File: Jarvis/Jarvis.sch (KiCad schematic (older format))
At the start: 180 parts, among them IC1 ADP1607, IC2 MAX-8Q, IC3 MPU-9250, IC4 STM32F411CxUx, IC5 Si4460, IC6 MS5611-01BA03, IC7 S25FL127S, J1 PYRO, J2 PWR, J3 ARM, J4 MICROUSB, P1 SMA, P2 SMA, P3 SWD_TC, Q1 PFET, Q2 PFET, Q3 PFET, Q4 NFET, Q5 NFET, Q6 NFET, Q7 NFET, X1 434MHz ANT, X10 Housing x1, X11 Housing x3, X12 M Crimps x6, X13 F Crimps x17, X14 Crimp Tool, X15 RF Frame, X16 RF Cover, X2 Red LED, X3 AA Battery, X4 AA Holder, X5 ARM Switch, X6 Wire, X7 Heat Shrink, X8 Housing x1, X9 Housing x4, Y1 26MHz, Y2 30MHz

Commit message: Checked all Footprints
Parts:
- added X17, X18, X19: Heat Shrink, symbol PART
- C11: Farnell 2524673 -> 1414575
- C27: Farnell 1973025 -> 2496795
- D1, D2, D3: Farnell 1226372 -> 1328306
- D4: Farnell 1226390 -> 1328309
- IC7: footprint agg:WND008 -> agg:S25FL127S
- L1: footprint Inductors_NEOSID:Neosid_Inductor_SM-NE29_SMD1008 -> Library:VLF252012MT
- P2: Farnell 1608592 -> 1019325
- R10, R26, R29, R33, R34, R4, R5, R6, R8, R9: Farnell 1358015 -> 2072515
- X12: Farnell (none) -> 1830754
- X13: RS (none) -> 688-1381
- X6: Farnell (none) -> 2367724
- X7: Farnell (none) -> 1210349
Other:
- note added: "X1 434MHz Stubby Radio Antenna\nX2 Red Indicator LED for Pyro Arming\nX3 Energizer L91 Lithium Ultimate AA\nX4 AA Battery Holder\nX5 Key Switch for Arming Pyrotechnics\nX6 Wire\nX7 Black Heatshrink"
- note added: "X17 Red Heatshrink\nX18 Blue Heatshrink\nX19 Yellow Heatshrink"
- note removed: "TODO:"
- note removed: "TODO: Select Wire, Heatshrink & Crimps"
- note removed: "X1 434MHz Stubby Radio Antenna\nX2 Red Indicator LED for Pyro Arming\nX3 Energizer L91 Lithium Ultimate AA\nX4 AA Battery Holder\nX5 Key Switch for Arming Pyrotechnics\nX6 Wire\nX7 Heatshrink"
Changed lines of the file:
@@
 F 0 "L1" H 1630 990 50  0000 L CNN
 F 1 "2.2uH" H 1650 900 50  0000 L CNN
-F 2 "Inductors_NEOSID:Neosid_Inductor_SM-NE29_SMD1008" H 1600 950 50  0001 C CNN
+F 2 "Library:VLF252012MT" H 1600 950 50  0001 C CNN
 F 3 "http://www.farnell.com/datasheets/1759590.pdf" H 1600 950 50  0001 C CNN
 F 4 "2455292" H 1600 950 60  0001 C CNN "Farnell"
@@
 F 2 "agg:0402-L" H 2000 5800 50  0001 C CNN
 F 3 "http://www.farnell.com/datasheets/1729045.pdf" H 2000 5800 50  0001 C CNN
-F 4 "1358015" H 2000 5800 60  0001 C CNN "Farnell"
+F 4 "2072515" H 2000 5800 60  0001 C CNN "Farnell"
 	1    2000 5800
 	0    -1   1    0
@@
 Text Label 11700 4750 0    60   ~ 0
 PYRO3
-Text Notes 7550 9220 0    47   ~ 0
+Text Notes 8450 9220 0    47   ~ 0
 Camera will have its\nown power supply ect.
 $Comp
@@
 F 2 "agg:0603-LED" H 12650 4800 50  0001 C CNN
 F 3 "http://www.farnell.com/datasheets/1693302.pdf" H 12650 4800 50  0001 C CNN
-F 4 "1226372" H 12650 4800 60  0001 C CNN "Farnell"
+F 4 "1328306" H 12650 4800 60  0001 C CNN "Farnell"
 	1    12650 4800
 	0    -1   -1   0
@@
 F 2 "agg:0603-LED" H 15000 4800 50  0001 C CNN
 F 3 "http://www.farnell.com/datasheets/302470.pdf" H 15000 4800 50  0001 C CNN
-F 4 "1226390" H 15000 4800 60  0001 C CNN "Farnell"
+F 4 "1328309" H 15000 4800 60  0001 C CNN "Farnell"
 	1    15000 4800
 	0    -1   -1   0
@@
 F 2 "agg:0402-L" H 7300 6750 50  0001 C CNN
 F 3 "http://www.farnell.com/datasheets/1446011.pdf" H 7300 6750 50  0001 C CNN
-F 4 "1973025" H 7300 6750 60  0001 C CNN "Farnell"
+F 4 "2496795" H 7300 6750 60  0001 C CNN "Farnell"
 	1    7300 6750
 	1    0    0    -1
@@
 F 2 "Library:SMA-142-0701-801" H 8300 6600 60  0001 C CNN
 F 3 "http://www.farnell.com/datasheets/493539.pdf" H 8300 6600 60  0001 C CNN
-F 4 "1608592" H 8300 6600 60  0001 C CNN "Farnell"
+F 4 "1019325" H 8300 6600 60  0001 C CNN "Farnell"
 	1    8300 6600
 	1    0    0    1
@@
 F 2 "agg:0402-L" H 5200 3900 50  0001 C CNN
 F 3 "http://www.farnell.com/datasheets/2009679.pdf" H 5200 3900 50  0001 C CNN
-F 4 "2524673" H 5200 3900 60  0001 C CNN "Farnell"
+F 4 "1414575" H 5200 3900 60  0001 C CNN "Farnell"
 	1    5200 3900
 	-1   0    0    -1
@@
 F 2 "agg:0402-L" H 10050 7000 50  0001 C CNN
 F 3 "http://www.farnell.com/datasheets/1729045.pdf" H 10050 7000 50  0001 C CNN
-F 4 "1358015" H 10050 7000 60  0001 C CNN "Farnell"
+F 4 "2072515" H 10050 7000 60  0001 C CNN "Farnell"
 	1    10050 7000
 	0    -1   1    0
@@
 F 2 "agg:0402-L" H 10350 6600 50  0001 C CNN
 F 3 "http://www.farnell.com/datasheets/1729045.pdf" H 10350 6600 50  0001 C CNN
-F 4 "1358015" H 10350 6600 60  0001 C CNN "Farnell"
+F 4 "2072515" H 10350 6600 60  0001 C CNN "Farnell"
 	1    10350 6600
 	-1   0    0    -1
@@
 F 2 "agg:0603-LED" H 13450 4800 50  0001 C CNN
 F 3 "http://www.farnell.com/datasheets/1693302.pdf" H 13450 4800 50  0001 C CNN
-F 4 "1226372" H 13450 4800 60  0001 C CNN "Farnell"
+F 4 "1328306" H 13450 4800 60  0001 C CNN "Farnell"
 	1    13450 4800
 	0    -1   -1   0
@@
 F 2 "agg:0603-LED" H 14200 4800 50  0001 C CNN
 F 3 "http://www.farnell.com/datasheets/1693302.pdf" H 14200 4800 50  0001 C CNN
-F 4 "1226372" H 14200 4800 60  0001 C CNN "Farnell"
+F 4 "1328306" H 14200 4800 60  0001 C CNN "Farnell"
 	1    14200 4800
 	0    -1   -1   0
@@
 F 2 "agg:0402-L" H 9400 1600 50  0001 C CNN
 F 3 "http://www.farnell.com/datasheets/1729045.pdf" H 9400 1600 50  0001 C CNN
-F 4 "1358015" H 9400 1600 60  0001 C CNN "Farnell"
+F 4 "2072515" H 9400 1600 60  0001 C CNN "Farnell"
 	1    9400 1600
 	0    -1   -1   0
@@
 F 2 "agg:0402-L" H 11850 1600 50  0001 C CNN
 F 3 "http://www.farnell.com/datasheets/1729045.pdf" H 11850 1600 50  0001 C CNN
-F 4 "1358015" H 11850 1600 60  0001 C CNN "Farnell"
+F 4 "2072515" H 11850 1600 60  0001 C CNN "Farnell"
 	1    11850 1600
 	0    -1   -1   0
@@
 F 2 "agg:0402-L" H 14300 1600 50  0001 C CNN
 F 3 "http://www.farnell.com/datasheets/1729045.pdf" H 14300 1600 50  0001 C CNN
-F 4 "1358015" H 14300 1600 60  0001 C CNN "Farnell"
+F 4 "2072515" H 14300 1600 60  0001 C CNN "Farnell"
 	1    14300 1600
 	0    -1   -1   0
@@
 F 2 "agg:0402-L" H 14900 1300 50  0001 C CNN
 F 3 "http://www.farnell.com/datasheets/1729045.pdf" H 14900 1300 50  0001 C CNN
-F 4 "1358015" H 14900 1300 60  0001 C CNN "Farnell"
+F 4 "2072515" H 14900 1300 60  0001 C CNN "Farnell"
 	1    14900 1300
 	0    -1   1    0
@@
 F 2 "agg:0402-L" H 12450 1300 50  0001 C CNN
 F 3 "http://www.farnell.com/datasheets/1729045.pdf" H 12450 1300 50  0001 C CNN
-F 4 "1358015" H 12450 1300 60  0001 C CNN "Farnell"
+F 4 "2072515" H 12450 1300 60  0001 C CNN "Farnell"
 	1    12450 1300
 	0    -1   1    0
@@
 F 2 "agg:0402-L" H 10000 1300 50  0001 C CNN
 F 3 "http://www.farnell.com/datasheets/1729045.pdf" H 10000 1300 50  0001 C CNN
-F 4 "1358015" H 10000 1300 60  0001 C CNN "Farnell"
+F 4 "2072515" H 10000 1300 60  0001 C CNN "Farnell"
 	1    10000 1300
 	0    -1   1    0
@@
 	1    0    0    -1
 $EndComp
-Text Notes 7550 9460 0    47   ~ 0
+Text Notes 8450 9450 0    47   ~ 0
 Red 3mm LED wired in\nparallel with keyswitch\nto provide pyro status.
 Text Notes 4450 9550 0    47   ~ 0
-X1 434MHz Stubby Radio Antenna\nX2 Red Indicator LED for Pyro Arming\nX3 Energizer L91 Lithium Ultimate AA\nX4 AA Battery Holder\nX5 Key Switch for Arming Pyrotechnics\nX6 Wire\nX7 Heatshrink
+X1 434MHz Stubby Radio Antenna\nX2 Red Indicator LED for Pyro Arming\nX3 Energizer L91 Lithium Ultimate AA\nX4 AA Battery Holder\nX5 Key Switch for Arming Pyrotechnics\nX6 Wire\nX7 Black Heatshrink
 $Comp
 L CONN_01x03 J3
@@
 	0    -1   -1   0
 $EndComp
-Text Notes 7550 9050 0    55   ~ 11
+Text Notes 8450 9050 0    55   ~ 11
 Notes:
-Text Notes 7550 9700 0    47   ~ 0
+Text Notes 8450 9700 0    47   ~ 0
 External HBT & Status\nindication will be done\nthrough sounder & radio
 Text Notes 4451 9122 0    47   ~ 9
@@
 F 2 "" H 7150 8850 50  0001 C CNN
 F 3 "http://www.farnell.com/datasheets/621888.pdf" H 7150 8850 50  0001 C CNN
+F 4 "688-1381" H 7150 8850 60  0001 C CNN "RS"
 	1    7150 8850
 	1    0    0    -1
@@
 F 2 "" H 7150 8600 50  0001 C CNN
 F 3 "" H 7150 8600 50  0001 C CNN
+F 4 "2367724" H 7150 8600 60  0001 C CNN "Farnell"
 	1    7150 8600
 	1    0    0    -1
@@
 F 2 "" H 6600 8850 50  0001 C CNN
 F 3 "" H 6600 8850 50  0001 C CNN
+F 4 "1830754" H 6600 8850 60  0001 C CNN "Farnell"
 	1    6600 8850
 	1    0    0    -1
@@
 F 2 "" H 7700 8600 50  0001 C CNN
 F 3 "" H 7700 8600 50  0001 C CNN
+F 4 "1210349" H 7700 8600 60  0001 C CNN "Farnell"
 	1    7700 8600
 	1    0    0    -1
@@
 Text Notes 6051 9549 0    47   ~ 9
 X14
-Text Notes 6650 8250 0    60   Italic 0
-TODO: Select Wire, Heatshrink & Crimps
 $Comp
 L GND #PWR0101
@@
 	1    0    0    -1
 $EndComp
-Text Notes 6650 8250 0    60   Italic 12
-TODO:
 $Comp
 L ESD_DIODE D5
@@
 F 0 "IC7" H 14750 6900 50  0000 L CNN
 F 1 "S25FL127S" H 14750 6300 50  0000 L CNN
-F 2 "agg:WND008" H 14750 6200 50  0001 L CNN
+F 2 "agg:S25FL127S" H 14750 6200 50  0001 L CNN
 F 3 "https://www.spansion.com/Support/Datasheets/S25FL127S_00.pdf" H 14750 6100 50  0001 L CNN
 F 4 "2328003" H 14750 6000 50  0001 L CNN "Farnell"
@@
 F 2 "agg:0402-L" H 10550 6600 50  0001 C CNN
 F 3 "http://www.farnell.com/datasheets/1729045.pdf" H 10550 6600 50  0001 C CNN
-F 4 "1358015" H 10550 6600 60  0001 C CNN "Farnell"
+F 4 "2072515" H 10550 6600 60  0001 C CNN "Farnell"
 	1    10550 6600
 	1    0    0    -1
@@
 	11150 4450 11150 5000
 Wire Notes Line
-	8550 9800 500  9800
+	500  9800 9450 9800
 Wire Notes Line
 	4250 500  4250 9800
@@
 Wire Wire Line
 	1800 5600 2150 5600
-Wire Notes Line
-	8550 500  8550 9800
 Wire Wire Line
 	5950 7650 5950 7700
@@
 	1    0    0    -1
 $EndComp
+$Comp
+L PART X17
+U 1 1 571ECFBC
+P 8250 8600
+F 0 "X17" H 8300 8700 50  0000 L CNN
+F 1 "Heat Shrink" H 8300 8600 50  0000 L CNN
+F 2 "" H 8250 8600 50  0001 C CNN
+F 3 "" H 8250 8600 50  0001 C CNN
+F 4 "1210365" H 8250 8600 60  0001 C CNN "Farnell"
+	1    8250 8600
+	1    0    0    -1
+$EndComp
+$Comp
+L PART X18
+U 1 1 571ED208
+P 8800 8600
+F 0 "X18" H 8850 8700 50  0000 L CNN
+F 1 "Heat Shrink" H 8850 8600 50  0000 L CNN
+F 2 "" H 8800 8600 50  0001 C CNN
+F 3 "" H 8800 8600 50  0001 C CNN
+F 4 " 1210405" H 8800 8600 60  0001 C CNN "Farnell"
+	1    8800 8600
+	1    0    0    -1
+$EndComp
+$Comp
+L PART X19
+U 1 1 571ED451
+P 8250 8850
+F 0 "X19" H 8300 8950 50  0000 L CNN
+F 1 "Heat Shrink" H 8300 8850 50  0000 L CNN
+F 2 "" H 8250 8850 50  0001 C CNN
+F 3 "" H 8250 8850 50  0001 C CNN
+F 4 "1210381" H 8250 8850 60  0001 C CNN "Farnell"
+	1    8250 8850
+	1    0    0    -1
+$EndComp
+Wire Notes Line
+	8550 8100 8550 500
+Wire Notes Line
+	9450 9800 9450 8100
+Text Notes 8900 8300 0    60   Italic 0
+COMPLETE
+Text Notes 7000 9250 0    47   ~ 0
+X17 Red Heatshrink\nX18 Blue Heatshrink\nX19 Yellow Heatshrink
 $EndSCHEMATC

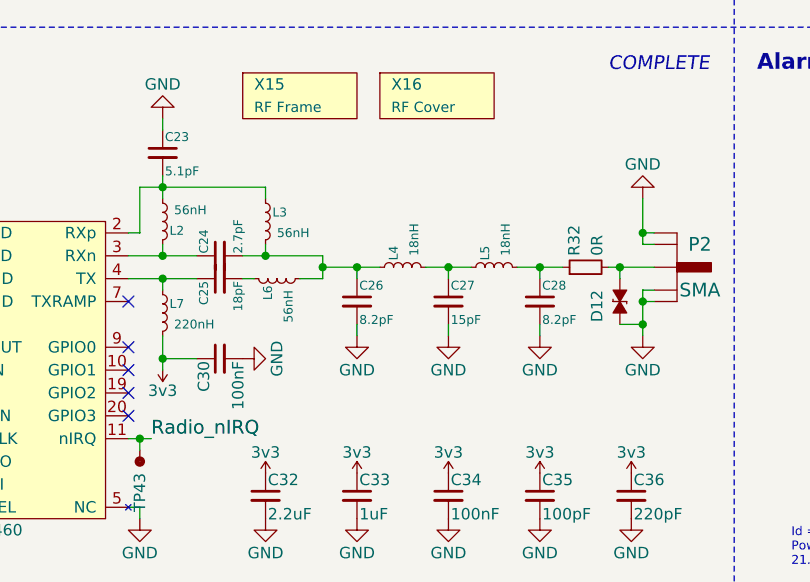
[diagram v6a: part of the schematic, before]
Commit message: Modified radio circuit to 868MHz and generated stickerBOM
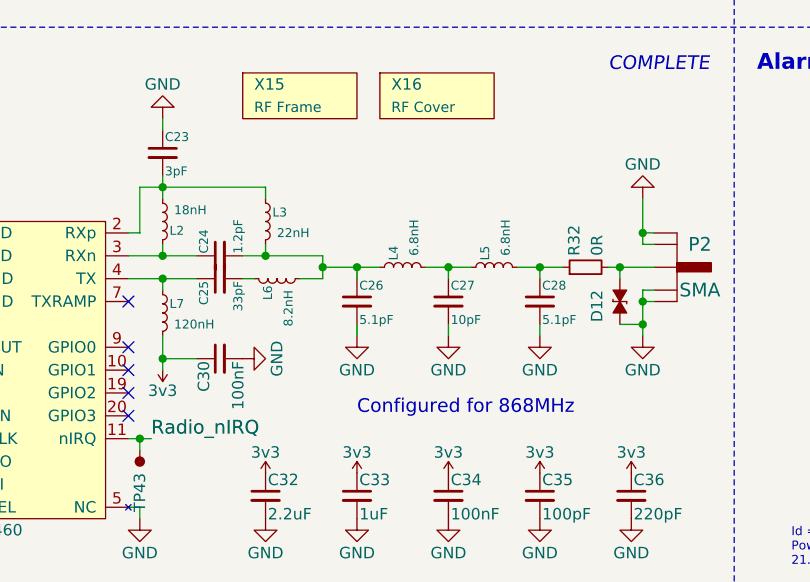
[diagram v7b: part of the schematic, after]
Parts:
- C23: value 5.1pF -> 3pF; Farnell 1885321 -> 2210752
- C24: value 2.7pF -> 1.2pF; Farnell 2310308 -> 2218843
- C25: value 18pF -> 33pF; Farnell 1885342 -> 2434643
- C26, C28: value 8.2pF -> 5.1pF; Farnell 2310320 -> 1885321
- C27: value 15pF -> 10pF; Farnell 2496795 -> 1758941
- L2: value 56nH -> 18nH; Farnell 1669639 -> 1865775
- L3: value 56nH -> 22nH; Farnell 1669639 -> 1669580
- L4, L5: value 18nH -> 6.8nH; Farnell 1760988 -> 1711736
- L6: value 56nH -> 8.2nH; Farnell 1669639 -> 1865771
- L7: value 220nH -> 120nH; Farnell 2215631 -> 2424731
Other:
- note added: "Configured for 868MHz"
